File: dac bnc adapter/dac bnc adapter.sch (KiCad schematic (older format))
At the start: 10 parts

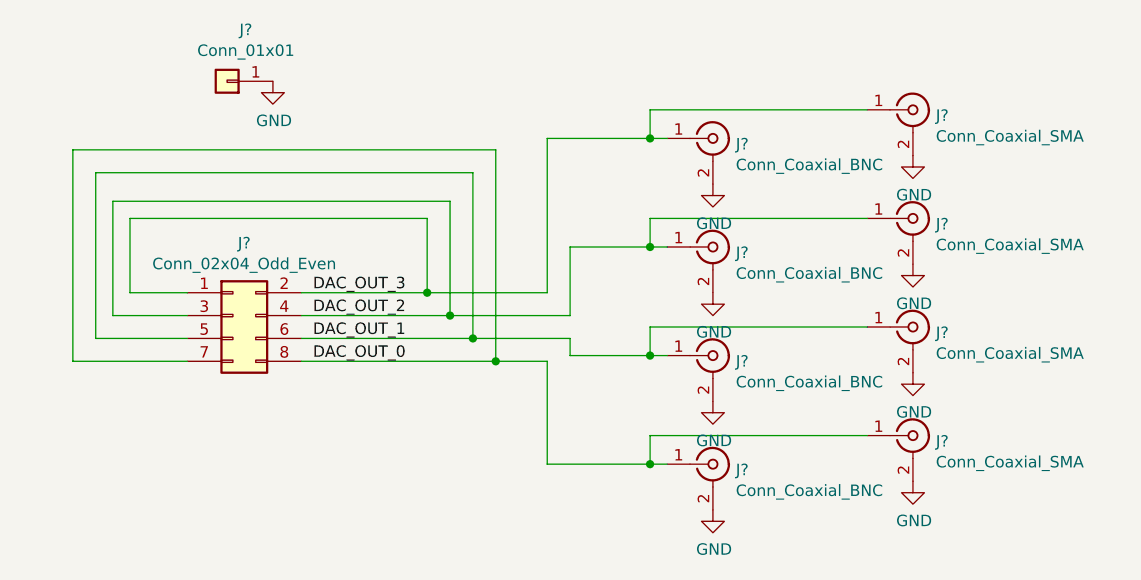
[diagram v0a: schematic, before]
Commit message: DAC BNC Adapter: removed BNC connectors, finished layout
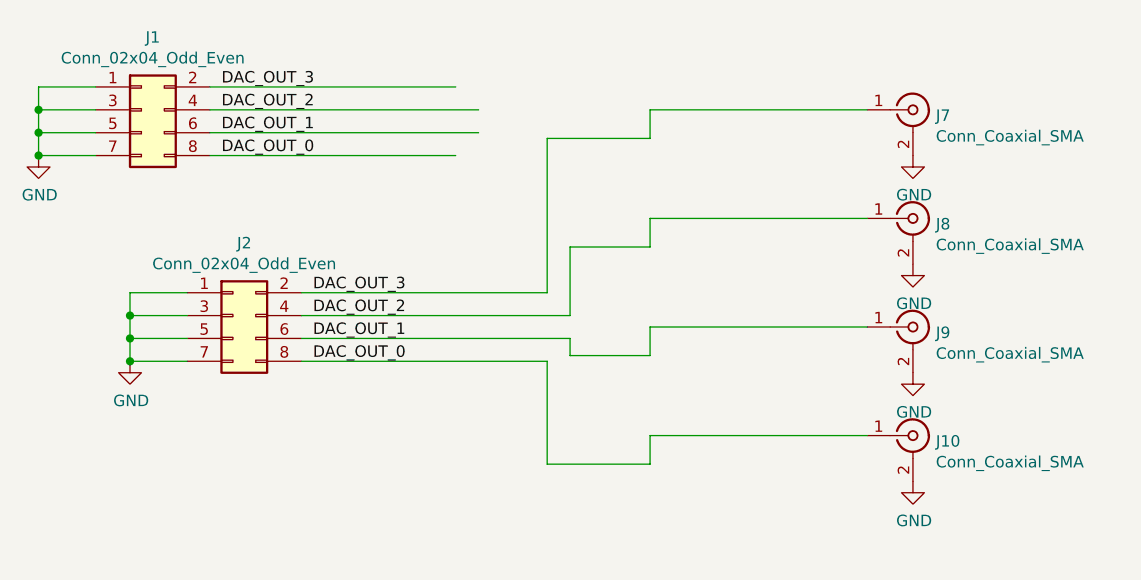
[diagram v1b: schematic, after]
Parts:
- removed J? (x4): Conn_Coaxial_BNC, symbol Connector:Conn_Coaxial
- removed J?: Conn_01x01, symbol Connector_Generic:Conn_01x01
- added J1: Conn_02x04_Odd_Even, Connector_PinHeader_2.54mm:PinHeader_2x04_P2.54mm_Vertical, symbol Connector_Generic:Conn_02x04_Odd_Even
- J10, J7, J8, J9: renamed from J?; footprint (none) -> Connector_Coaxial:SMA_Amphenol_132134_Vertical
- J2: renamed from J?; footprint (none) -> Connector_PinHeader_2.54mm:PinHeader_2x04_P2.54mm_Vertical
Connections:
- wire segments 44 -> 38
